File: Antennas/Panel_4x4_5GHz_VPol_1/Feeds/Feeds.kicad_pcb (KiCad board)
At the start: 2 copper layers, 186 x 226 mm, 89 parts

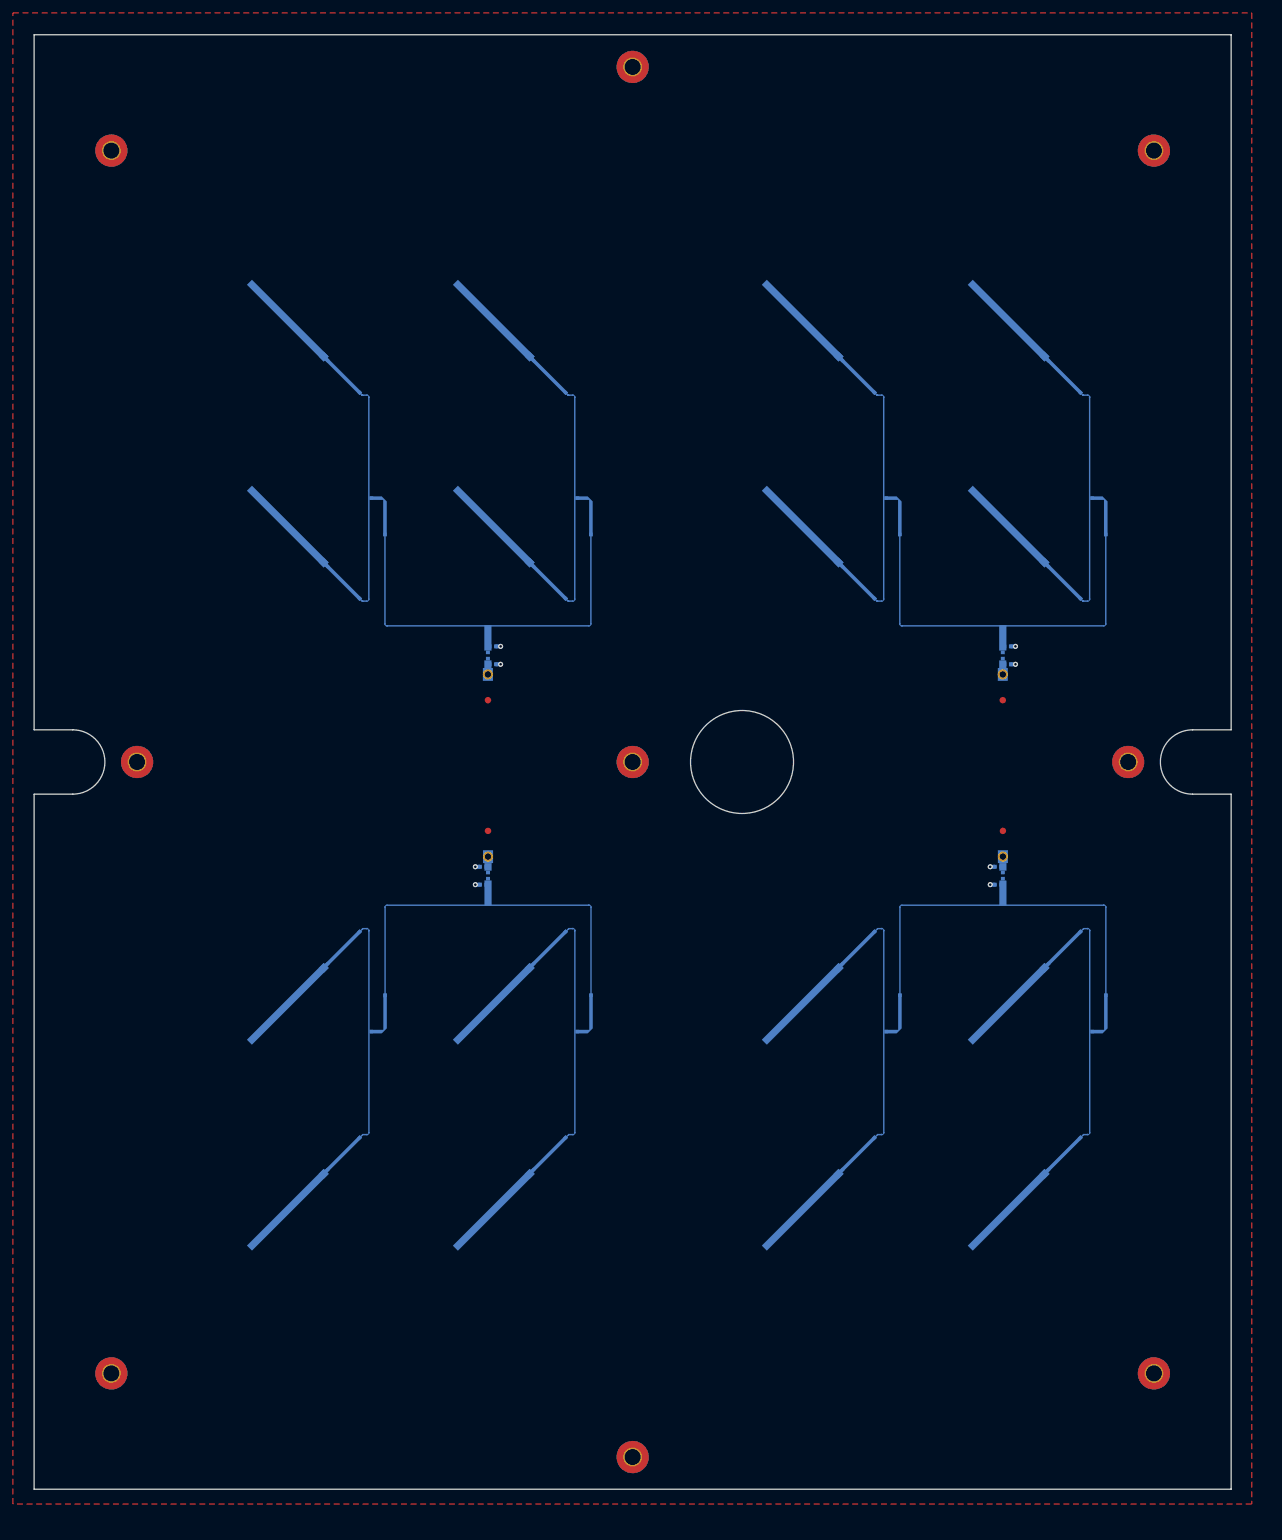
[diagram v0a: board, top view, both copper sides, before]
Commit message: Add new single polarity aperture coupled 4x4 antenna. RasPiCNM4Connector test Gerbers for PCBWay Cleanups and optimixations for AP3500
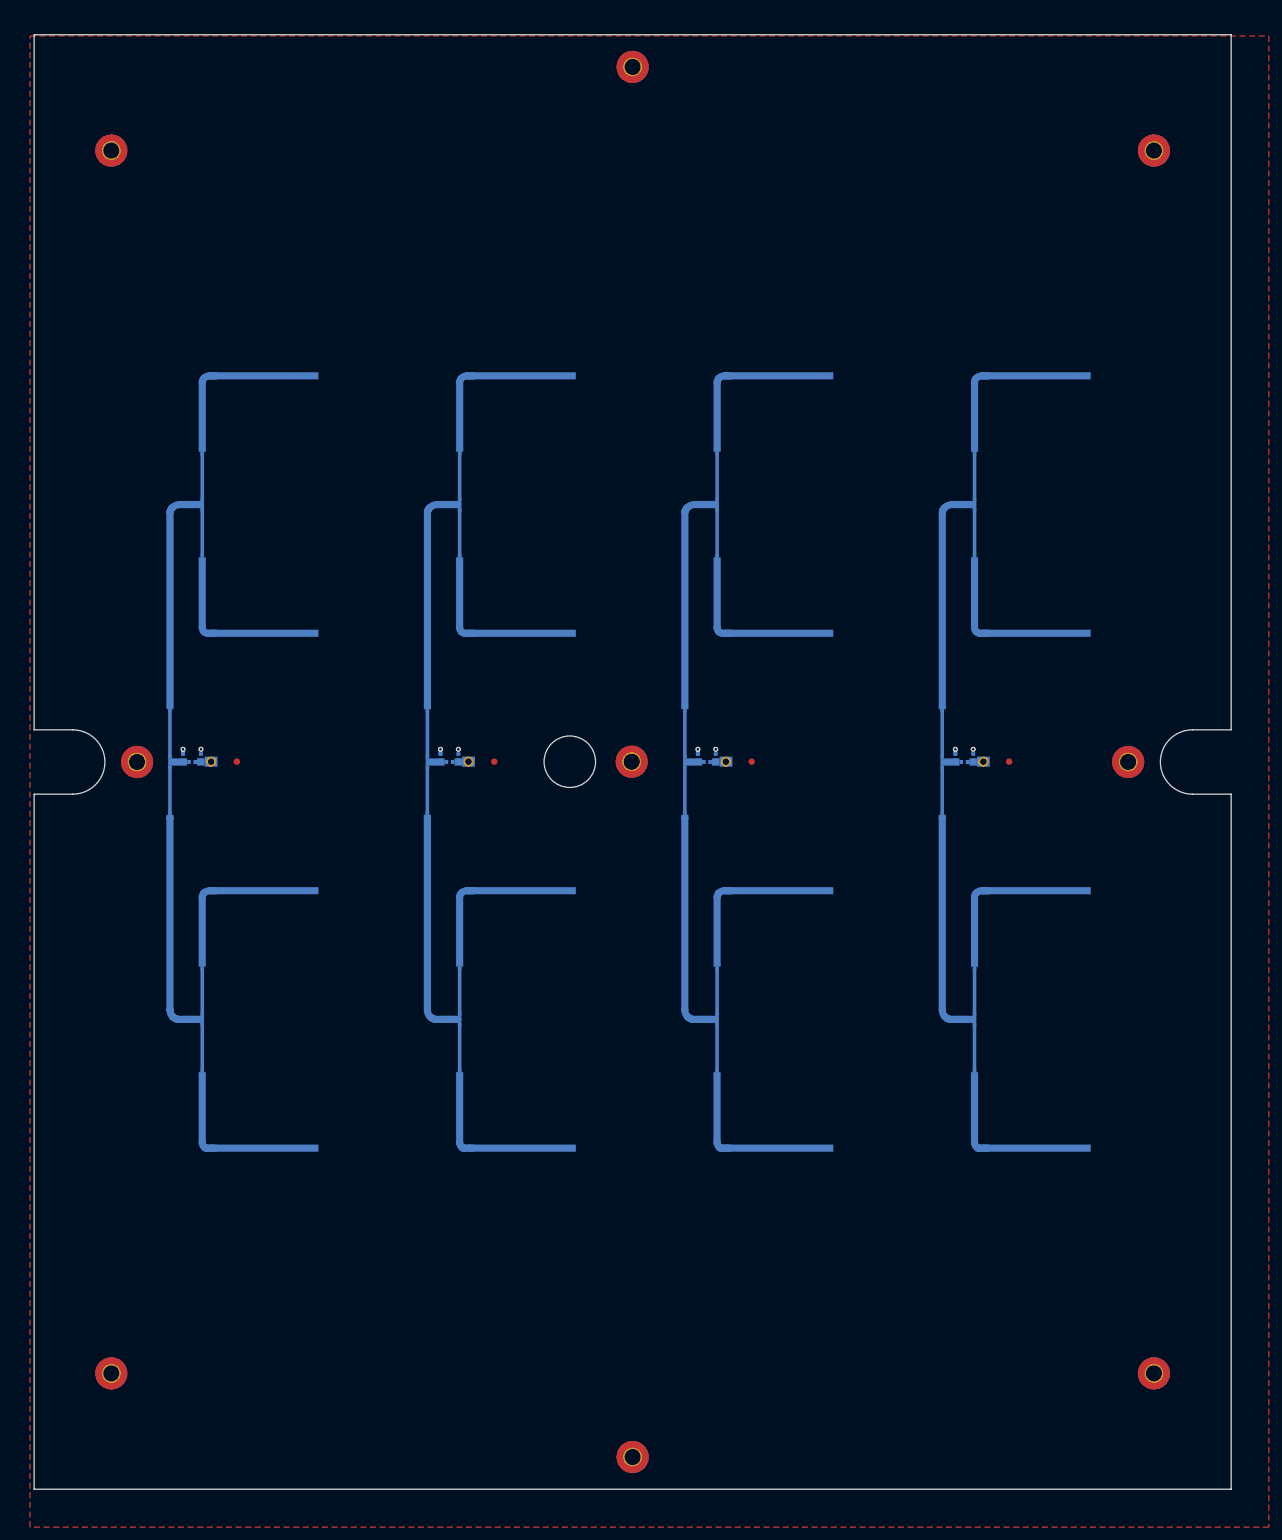
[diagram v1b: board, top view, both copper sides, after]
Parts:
- removed the >NAME at (149.8, 129.3)
- removed the >NAME at (70.5, 130.6)
- removed the >NAME at (71.3, 95.0)
- removed the >NAME at (151.3, 95.0)
- removed the >NAME at (150.5, 130.6)
- removed the >NAME at (69.8, 129.3)
- removed the >NAME at (69.8, 132.1)
- removed the >NAME at (151.3, 97.8)
- removed the >NAME at (150.5, 96.5)
- removed the >NAME at (149.8, 132.1)
- removed the >NAME at (71.3, 97.8)
- removed the >NAME at (70.5, 96.5)
- removed the AE5 at (35.0, 187.0)
- removed the AE5 at (67.0, 72.0)
- removed the AE5 at (115.0, 72.0)
- removed the AE5 at (115.0, 40.0)
- removed the AE5 at (67.0, 187.0)
- removed the AE5 at (67.0, 155.0)
- removed the AE5 at (35.0, 155.0)
- removed the AE5 at (147.0, 40.0)
- removed the AE5 at (67.0, 40.0)
- removed the AE5 at (147.0, 155.0)
- removed the AE5 at (147.0, 72.0)
- removed the AE5 at (147.0, 187.0)
- removed the AE5 at (35.0, 40.0)
- removed the AE5 at (35.0, 72.0)
- removed the AE5 at (115.0, 187.0)
- removed the AE5 at (115.0, 155.0)
- removed Feed1: Feed1, Scott:Flat_Ant_Hole
- removed Feed2: Feed2, Scott:Flat_Ant_Hole
- removed Feed3: Feed3, Scott:Flat_Ant_Hole
- removed the Feed4 at (70.5, 127.7)
- removed the REF** at (164.0, 138.9)
- removed the REF** at (86.5, 154.9)
- removed the REF** at (157.6, 82.6)
- removed the REF** at (45.6, 144.4)
- removed the REF** at (54.5, 72.0)
- removed the REF** at (84.0, 56.0)
- removed the REF** at (84.0, 88.0)
- removed the REF** at (54.5, 154.9)
- removed the REF** at (166.5, 91.8)
- removed the REF** at (125.6, 176.4)
- removed the REF** at (45.6, 82.6)
- removed the REF** at (86.5, 135.3)
- removed the REF** at (84.0, 170.9)
- removed the REF** at (52.0, 88.0)
- removed the REF** at (45.6, 176.4)
- removed the REF** at (86.5, 72.0)
- removed the REF** at (164.0, 170.9)
- removed the REF** at (54.5, 135.3)
- removed the REF** at (52.0, 170.9)
- removed the REF** at (134.5, 91.8)
- removed the REF** at (134.5, 135.3)
- removed the REF** at (134.5, 72.0)
- removed the REF** at (132.0, 88.0)
- removed the REF** at (166.5, 135.3)
- removed the REF** at (52.0, 56.0)
- removed the REF** at (86.5, 91.8)
- removed the REF** at (132.0, 56.0)
- removed the REF** at (125.6, 82.6)
- removed the REF** at (164.0, 56.0)
- removed the REF** at (77.6, 144.4)
- removed the REF** at (134.5, 154.9)
- removed the REF** at (157.6, 176.4)
- removed the REF** at (125.6, 50.6)
- removed the REF** at (166.5, 154.9)
- removed the REF** at (166.5, 72.0)
- removed the REF** at (45.6, 50.6)
- removed the REF** at (132.0, 138.9)
- removed the REF** at (157.6, 144.4)
- removed the REF** at (157.6, 50.6)
- removed the REF** at (132.0, 170.9)
- removed the REF** at (77.6, 82.6)
- removed the REF** at (54.5, 91.8)
- removed the REF** at (125.6, 144.4)
- removed the REF** at (77.6, 50.6)
- removed the REF** at (84.0, 138.9)
- removed the REF** at (77.6, 176.4)
- removed the REF** at (52.0, 138.9)
- removed the REF** at (164.0, 88.0)
- added >NAME: >VALUE, Scott-RF-JLCPCB-600um7628-2layer:C_0402_1005Metric, B.Cu at (143.1, 112.2)
- added >NAME: >VALUE, Scott-RF-JLCPCB-600um7628-2layer:C_0402_1005Metric, B.Cu at (145.9, 112.2)
- added >NAME: >VALUE, Scott-RF-JLCPCB-600um7628-2layer:C_0402_1005Metric, B.Cu at (64.6, 113.0)
- added >NAME: >VALUE, Scott-RF-JLCPCB-600um7628-2layer:C_0402_1005Metric, B.Cu at (144.6, 113.0)
- added >NAME: >VALUE, Scott-RF-JLCPCB-600um7628-2layer:C_0402_1005Metric, B.Cu at (103.1, 112.2)
- added >NAME: >VALUE, Scott-RF-JLCPCB-600um7628-2layer:C_0402_1005Metric, B.Cu at (63.1, 112.2)
- added >NAME: >VALUE, Scott-RF-JLCPCB-600um7628-2layer:C_0402_1005Metric, B.Cu at (24.6, 113.0)
- added >NAME: >VALUE, Scott-RF-JLCPCB-600um7628-2layer:C_0402_1005Metric, B.Cu at (104.6, 113.0)
- added >NAME: >VALUE, Scott-RF-JLCPCB-600um7628-2layer:C_0402_1005Metric, B.Cu at (65.9, 112.2)
- added >NAME: >VALUE, Scott-RF-JLCPCB-600um7628-2layer:C_0402_1005Metric, B.Cu at (105.9, 112.2)
- added >NAME: >VALUE, Scott-RF-JLCPCB-600um7628-2layer:C_0402_1005Metric, B.Cu at (25.9, 112.2)
- added >NAME: >VALUE, Scott-RF-JLCPCB-600um7628-2layer:C_0402_1005Metric, B.Cu at (23.1, 112.2)
- added AE5: Antenna, Scott-RF-JLCPCB-600um7628-2layer:Feed_5.5_Linear_ApertureCoupled, F.Cu at (162.0, 53.0)
- added AE5: Antenna, Scott-RF-JLCPCB-600um7628-2layer:Feed_5.5_Linear_ApertureCoupled, F.Cu at (82.0, 93.0)
- added AE5: Antenna, Scott-RF-JLCPCB-600um7628-2layer:Feed_5.5_Linear_ApertureCoupled, F.Cu at (122.0, 133.0)
- added AE5: Antenna, Scott-RF-JLCPCB-600um7628-2layer:Feed_5.5_Linear_ApertureCoupled, F.Cu at (122.0, 173.0)
- added AE5: Antenna, Scott-RF-JLCPCB-600um7628-2layer:Feed_5.5_Linear_ApertureCoupled, F.Cu at (42.0, 173.0)
- added AE5: Antenna, Scott-RF-JLCPCB-600um7628-2layer:Feed_5.5_Linear_ApertureCoupled, F.Cu at (42.0, 133.0)
- added AE5: Antenna, Scott-RF-JLCPCB-600um7628-2layer:Feed_5.5_Linear_ApertureCoupled, F.Cu at (82.0, 133.0)
- added AE5: Antenna, Scott-RF-JLCPCB-600um7628-2layer:Feed_5.5_Linear_ApertureCoupled, F.Cu at (162.0, 133.0)
- added AE5: Antenna, Scott-RF-JLCPCB-600um7628-2layer:Feed_5.5_Linear_ApertureCoupled, F.Cu at (82.0, 53.0)
- added AE5: Antenna, Scott-RF-JLCPCB-600um7628-2layer:Feed_5.5_Linear_ApertureCoupled, F.Cu at (122.0, 93.0)
- added AE5: Antenna, Scott-RF-JLCPCB-600um7628-2layer:Feed_5.5_Linear_ApertureCoupled, F.Cu at (82.0, 173.0)
- added AE5: Antenna, Scott-RF-JLCPCB-600um7628-2layer:Feed_5.5_Linear_ApertureCoupled, F.Cu at (162.0, 93.0)
- added AE5: Antenna, Scott-RF-JLCPCB-600um7628-2layer:Feed_5.5_Linear_ApertureCoupled, F.Cu at (122.0, 53.0)
- added AE5: Antenna, Scott-RF-JLCPCB-600um7628-2layer:Feed_5.5_Linear_ApertureCoupled, F.Cu at (42.0, 93.0)
- added AE5: Antenna, Scott-RF-JLCPCB-600um7628-2layer:Feed_5.5_Linear_ApertureCoupled, F.Cu at (162.0, 173.0)
- added AE5: Antenna, Scott-RF-JLCPCB-600um7628-2layer:Feed_5.5_Linear_ApertureCoupled, F.Cu at (42.0, 53.0)
- added Feed4: Feed4, Scott:Flat_Ant_Hole, B.Cu at (107.5, 113.0)
- added Feed4: Feed4, Scott:Flat_Ant_Hole, B.Cu at (67.5, 113.0)
- added Feed4: Feed4, Scott:Flat_Ant_Hole, B.Cu at (147.5, 113.0)
- added Feed4: Feed4, Scott:Flat_Ant_Hole, B.Cu at (27.5, 113.0)
- added REF**: RF-Transformer-70.71ohm-Straight, Scott-RF-JLCPCB-600um7628-2layer:RF-Transformer-70.71ohm-Straight, B.Cu at (146.1, 152.2)
- added REF**: RF-Transformer-70.71ohm-Straight, Scott-RF-JLCPCB-600um7628-2layer:RF-Transformer-70.71ohm-Straight, B.Cu at (101.1, 112.2)
- added REF**: RF-Transformer-70.71ohm-Straight, Scott-RF-JLCPCB-600um7628-2layer:RF-Transformer-70.71ohm-Straight, B.Cu at (101.1, 113.8)
- added REF**: RF-Transformer-70.71ohm-Straight, Scott-RF-JLCPCB-600um7628-2layer:RF-Transformer-70.71ohm-Straight, B.Cu at (66.1, 152.2)
- added REF**: RF-Transformer-70.71ohm-Straight, Scott-RF-JLCPCB-600um7628-2layer:RF-Transformer-70.71ohm-Straight, B.Cu at (106.1, 153.8)
- added REF**: RF-Transformer-70.71ohm-Straight, Scott-RF-JLCPCB-600um7628-2layer:RF-Transformer-70.71ohm-Straight, B.Cu at (141.1, 112.2)
- added REF**: RF-Transformer-70.71ohm-Straight, Scott-RF-JLCPCB-600um7628-2layer:RF-Transformer-70.71ohm-Straight, B.Cu at (106.1, 73.8)
- added REF**: RF-Transformer-70.71ohm-Straight, Scott-RF-JLCPCB-600um7628-2layer:RF-Transformer-70.71ohm-Straight, B.Cu at (106.1, 152.2)
- added REF**: RF-Transformer-70.71ohm-Straight, Scott-RF-JLCPCB-600um7628-2layer:RF-Transformer-70.71ohm-Straight, B.Cu at (66.1, 72.2)
- added REF**: RF-Transformer-70.71ohm-Straight, Scott-RF-JLCPCB-600um7628-2layer:RF-Transformer-70.71ohm-Straight, B.Cu at (61.1, 112.2)
- added REF**: RF-Transformer-70.71ohm-Straight, Scott-RF-JLCPCB-600um7628-2layer:RF-Transformer-70.71ohm-Straight, B.Cu at (26.1, 152.2)
- added REF**: RF-Transformer-70.71ohm-Straight, Scott-RF-JLCPCB-600um7628-2layer:RF-Transformer-70.71ohm-Straight, B.Cu at (146.1, 153.8)
- added REF**: RF-Transformer-70.71ohm-Straight, Scott-RF-JLCPCB-600um7628-2layer:RF-Transformer-70.71ohm-Straight, B.Cu at (66.1, 153.8)
- added REF**: RF-Transformer-70.71ohm-Straight, Scott-RF-JLCPCB-600um7628-2layer:RF-Transformer-70.71ohm-Straight, B.Cu at (141.1, 113.8)
- added REF**: RF-Transformer-70.71ohm-Straight, Scott-RF-JLCPCB-600um7628-2layer:RF-Transformer-70.71ohm-Straight, B.Cu at (21.1, 112.2)
- added REF**: RF-Transformer-70.71ohm-Straight, Scott-RF-JLCPCB-600um7628-2layer:RF-Transformer-70.71ohm-Straight, B.Cu at (146.1, 73.8)
- added REF**: RF-Transformer-70.71ohm-Straight, Scott-RF-JLCPCB-600um7628-2layer:RF-Transformer-70.71ohm-Straight, B.Cu at (106.1, 72.2)
- added REF**: RF-Transformer-70.71ohm-Straight, Scott-RF-JLCPCB-600um7628-2layer:RF-Transformer-70.71ohm-Straight, B.Cu at (146.1, 72.2)
- added REF**: RF-Transformer-70.71ohm-Straight, Scott-RF-JLCPCB-600um7628-2layer:RF-Transformer-70.71ohm-Straight, B.Cu at (26.1, 73.8)
- added REF**: RF-Transformer-70.71ohm-Straight, Scott-RF-JLCPCB-600um7628-2layer:RF-Transformer-70.71ohm-Straight, B.Cu at (26.1, 72.2)
- added REF**: RF-Transformer-70.71ohm-Straight, Scott-RF-JLCPCB-600um7628-2layer:RF-Transformer-70.71ohm-Straight, B.Cu at (21.1, 113.8)
- added REF**: RF-Transformer-70.71ohm-Straight, Scott-RF-JLCPCB-600um7628-2layer:RF-Transformer-70.71ohm-Straight, B.Cu at (26.1, 153.8)
- added REF**: RF-Transformer-70.71ohm-Straight, Scott-RF-JLCPCB-600um7628-2layer:RF-Transformer-70.71ohm-Straight, B.Cu at (61.1, 113.8)
- added REF**: RF-Transformer-70.71ohm-Straight, Scott-RF-JLCPCB-600um7628-2layer:RF-Transformer-70.71ohm-Straight, B.Cu at (66.1, 73.8)
- moved H12 0.15 mm to (92.9, 113.0)
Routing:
- net /A1E5: track 0.00 -> 504.8 mm
- net /A1E3: track 250.9 -> 0.00 mm
- net (no net): track 129.4 -> 0.00 mm
- net /A1P1: track 125.2 -> 0.00 mm
- net GND: track 5.77 -> 2.82 mm
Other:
- outline, holes or cut-outs redrawn
